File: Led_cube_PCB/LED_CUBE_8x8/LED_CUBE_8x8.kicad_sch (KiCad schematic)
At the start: 0 parts

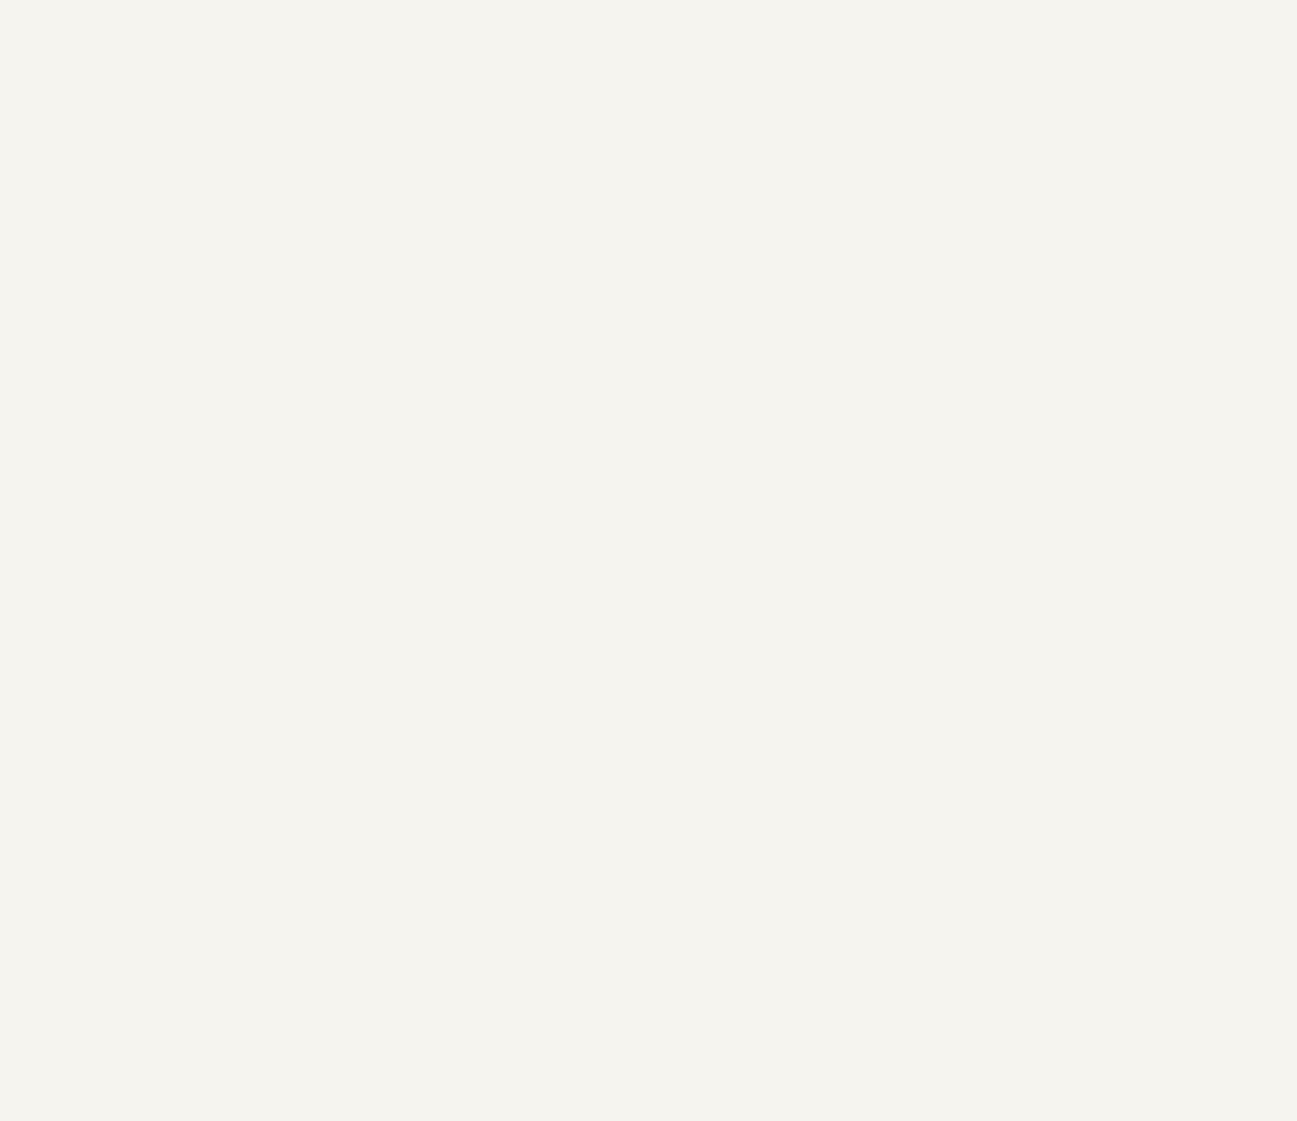
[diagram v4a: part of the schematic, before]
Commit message: added 3.3V power supply for microcontroller and started on STM schematic.
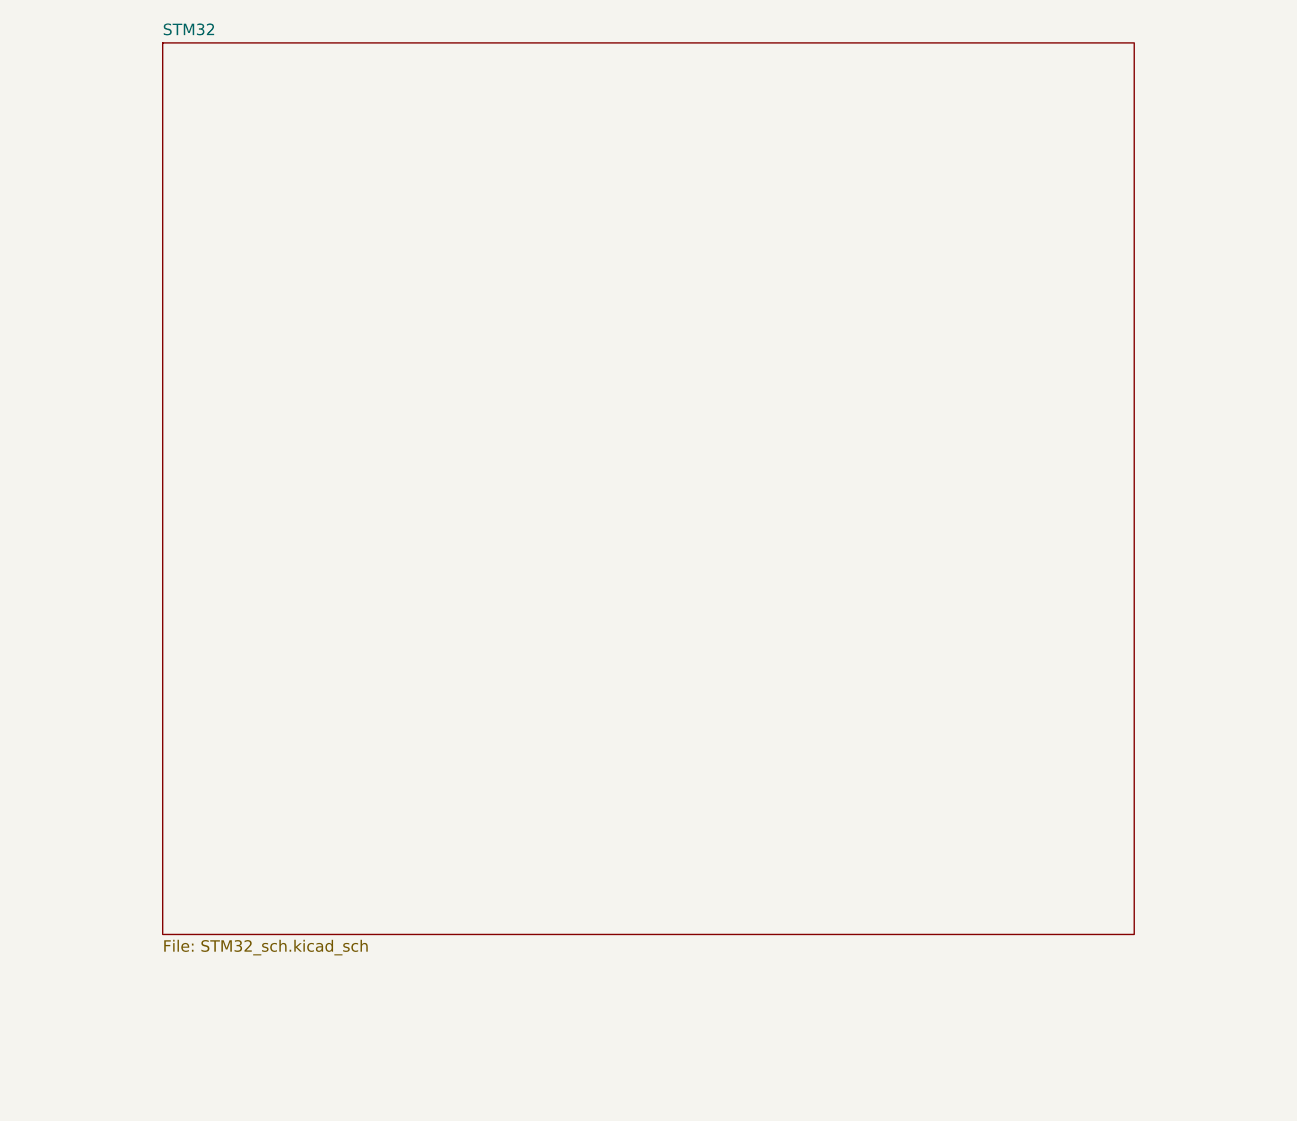
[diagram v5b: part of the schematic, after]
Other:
- added sheet STM32 (STM32_sch.kicad_sch)
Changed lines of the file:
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@@
+	)
+	(sheet
+		(at 93.98 22.86)
+		(size 107.95 99.06)
+		(exclude_from_sim no)
+		(in_bom yes)
+		(on_board yes)
+		(dnp no)
+		(fields_autoplaced yes)
+		(stroke
+			(width 0.1524)
+			(type solid)
+		)
+		(fill
+			(color 0 0 0 0.0000)
+		)
+		(property "Sheetname" "STM32"
+			(at 93.98 22.1484 0)
+			(effects
+				(font
+					(size 1.27 1.27)
+				)
+				(justify left bottom)
+			)
+		)
+		(property "Sheetfile" "STM32_sch.kicad_sch"
+			(at 93.98 122.5046 0)
+			(effects
+				(font
+					(size 1.27 1.27)
+				)
+				(justify left top)
+			)
+		)
+		(instances
+			(project "LED_CUBE_8x8"
+				(path "/b239677e-e361-4439-8200-63fb41f7e03c"
+					(page "6")
+				)
+			)
+		)
 	)
 	(sheet

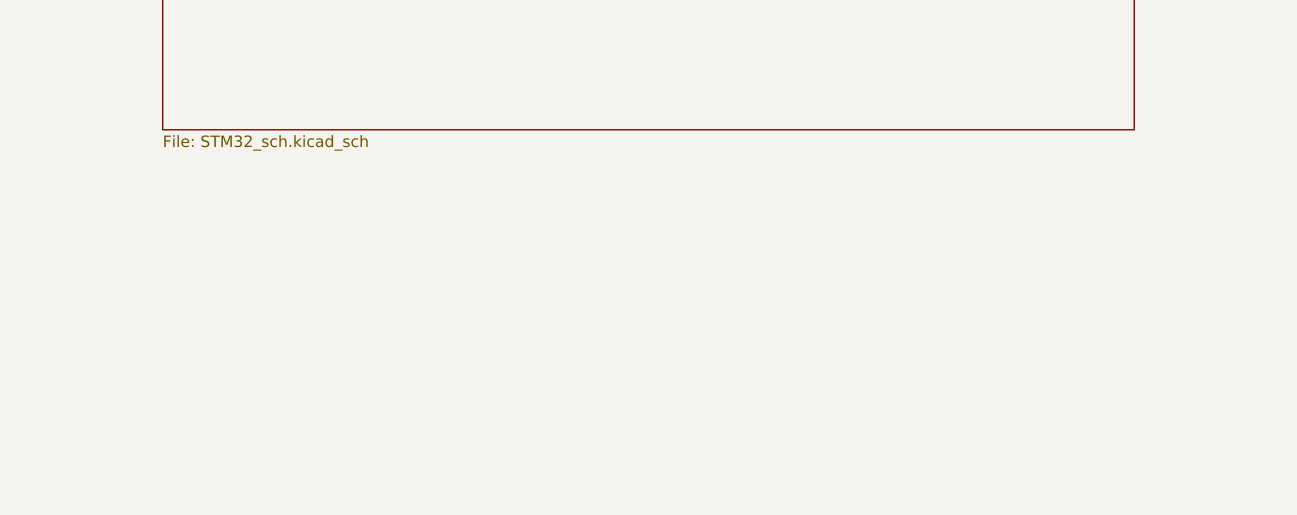
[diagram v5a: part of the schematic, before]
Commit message: WIP: added layer select schematic
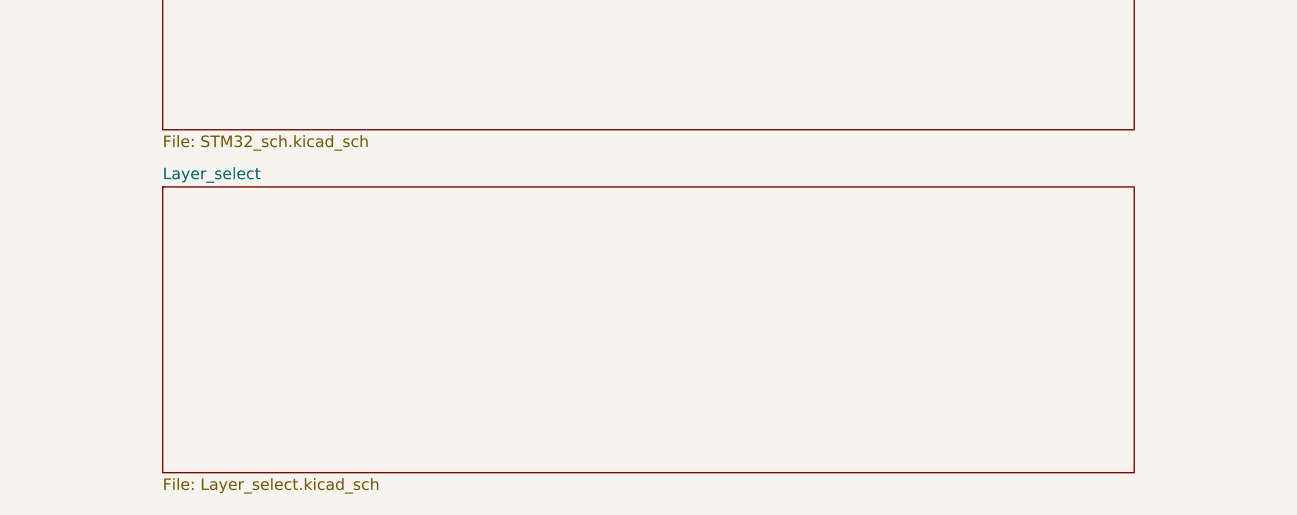
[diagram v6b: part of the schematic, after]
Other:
- added sheet Layer_select (Layer_select.kicad_sch)
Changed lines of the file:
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@@
+	)
+	(sheet
+		(at 93.98 128.27)
+		(size 107.95 31.75)
+		(exclude_from_sim no)
+		(in_bom yes)
+		(on_board yes)
+		(dnp no)
+		(fields_autoplaced yes)
+		(stroke
+			(width 0.1524)
+			(type solid)
+		)
+		(fill
+			(color 0 0 0 0.0000)
+		)
+		(property "Sheetname" "Layer_select"
+			(at 93.98 127.5584 0)
+			(effects
+				(font
+					(size 1.27 1.27)
+				)
+				(justify left bottom)
+			)
+		)
+		(property "Sheetfile" "Layer_select.kicad_sch"
+			(at 93.98 160.6046 0)
+			(effects
+				(font
+					(size 1.27 1.27)
+				)
+				(justify left top)
+			)
+		)
+		(instances
+			(project "LED_CUBE_8x8"
+				(path "/b239677e-e361-4439-8200-63fb41f7e03c"
+					(page "7")
+				)
+			)
+		)
 	)
 	(sheet
